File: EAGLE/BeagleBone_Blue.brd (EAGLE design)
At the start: 86.4 x 54.6 mm, 306 parts, among them J2 SERVO_HEADERS_8X, M1 JST_ZH_2, M2 JST_ZH_2, M3 JST_ZH_2, M4 JST_ZH_2, Q1 MOSFET-N, T1 BSS138W-7-F, T2 BSS138W-7-F, U1 TCAN1051HV, U10 TXS0108ERGYR, U13 EMMC, U2 SN74LV1T126DBVR, U3 TPD4S012DRY, U4 TPD4S012DRY, U5 24LC_32AT-I/OT, U6 SN74LVC1G07_DCK_5, U7 WL1835MODGBMOCT, U9 TXS0108ERGYR, X2 SCHA5B0200, X3 USB1, X4 10118192-0001LF, Y1 24 MHz, Y2 32.768kHz

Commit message: EAGLE: more attempts to consolidate library
I tried to rename some parts to eliminate the prefixes added by the exp-lbrs.ulp script.
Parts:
- 0, 1, 2, 3, BT, G, ON, R, WL: device BeagleBone_Blue:LED-0603 -> BeagleBone_Blue:BEAGLEBONE_BLUE_LED-0603
- 5VREG: device BeagleBone_Blue:SO08-TIGHT -> BeagleBone_Blue:BEAGLEBONE_BLUE_SO08-TIGHT
- SIP: device BeagleBone_Blue:OSD3358 -> BeagleBone_Blue:BEAGLEBONE_BLUE_OSD3358
- TP11, TP2, TP3, TP4, TP6, TP7, TP8, TP9: device BeagleBone_Blue:B0,65 -> BeagleBone_Blue:BEAGLEBONE_BLUE_B0,65
- U1: device BeagleBone_Blue:D8 -> BeagleBone_Blue:BEAGLEBONE_BLUE_D8
- U2: device BeagleBone_Blue:SOT23-5 -> BeagleBone_Blue:BEAGLEBONE_BLUE_SOT23-5
- U6: device BeagleBone_Blue:DCK5 -> BeagleBone_Blue:BEAGLEBONE_BLUE_DCK5

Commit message: BRD: update D1, D2, D3 footprints
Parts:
- D1: device adafruit:SOD-123 -> BeagleBone_Blue:ADAFRUIT_SOD-123FL
- D2, D3: device adafruit:SOD-123 -> adafruit:SOD-123FL
- moved D1 12.8 mm to (53.2, 3.17)
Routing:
- net GND: track 226.8 -> 226.2 mm
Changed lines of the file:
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@@
 <grid distance="5" unitdist="mil" unit="mm" style="lines" multiple="1" display="yes" altdistance="0.25" altunitdist="mil" altunit="mm"/>
 <layers>
-<layer number="1" name="Top" color="4" fill="1" visible="no" active="yes"/>
+<layer number="1" name="Top" color="4" fill="1" visible="yes" active="yes"/>
 <layer number="2" name="Route2" color="1" fill="3" visible="no" active="yes"/>
 <layer number="3" name="Route3" color="4" fill="3" visible="no" active="no"/>
@@
 <layer number="14" name="Route14" color="1" fill="6" visible="no" active="no"/>
 <layer number="15" name="Route15" color="4" fill="6" visible="no" active="yes"/>
-<layer number="16" name="Bottom" color="1" fill="1" visible="yes" active="yes"/>
+<layer number="16" name="Bottom" color="1" fill="1" visible="no" active="yes"/>
 <layer number="17" name="Pads" color="2" fill="1" visible="yes" active="yes"/>
 <layer number="18" name="Vias" color="2" fill="1" visible="yes" active="yes"/>
 <layer number="19" name="Unrouted" color="6" fill="1" visible="yes" active="yes"/>
 <layer number="20" name="Dimension" color="15" fill="1" visible="yes" active="yes"/>
-<layer number="21" name="tPlace" color="7" fill="1" visible="no" active="yes"/>
-<layer number="22" name="bPlace" color="7" fill="1" visible="yes" active="yes"/>
-<layer number="23" name="tOrigins" color="15" fill="1" visible="no" active="yes"/>
-<layer number="24" name="bOrigins" color="15" fill="1" visible="yes" active="yes"/>
+<layer number="21" name="tPlace" color="7" fill="1" visible="yes" active="yes"/>
+<layer number="22" name="bPlace" color="7" fill="1" visible="no" active="yes"/>
+<layer number="23" name="tOrigins" color="15" fill="1" visible="yes" active="yes"/>
+<layer number="24" name="bOrigins" color="15" fill="1" visible="no" active="yes"/>
 <layer number="25" name="tNames" color="7" fill="1" visible="no" active="yes"/>
 <layer number="26" name="bNames" color="7" fill="1" visible="no" active="yes"/>
@@
 <layer number="37" name="tTest" color="7" fill="1" visible="no" active="yes"/>
 <layer number="38" name="bTest" color="7" fill="1" visible="no" active="yes"/>
-<layer number="39" name="tKeepout" color="4" fill="11" visible="no" active="yes"/>
-<layer number="40" name="bKeepout" color="1" fill="11" visible="yes" active="yes"/>
-<layer number="41" name="tRestrict" color="4" fill="10" visible="no" active="yes"/>
-<layer number="42" name="bRestrict" color="1" fill="10" visible="yes" active="yes"/>
+<layer number="39" name="tKeepout" color="4" fill="11" visible="yes" active="yes"/>
+<layer number="40" name="bKeepout" color="1" fill="11" visible="no" active="yes"/>
+<layer number="41" name="tRestrict" color="4" fill="10" visible="yes" active="yes"/>
+<layer number="42" name="bRestrict" color="1" fill="10" visible="no" active="yes"/>
 <layer number="43" name="vRestrict" color="2" fill="10" visible="no" active="yes"/>
 <layer number="44" name="Drills" color="7" fill="1" visible="no" active="yes"/>
@@
 <layer number="50" name="dxf" color="7" fill="1" visible="no" active="no"/>
 <layer number="51" name="tDocu" color="7" fill="1" visible="no" active="yes"/>
-<layer number="52" name="bDocu" color="7" fill="1" visible="yes" active="yes"/>
+<layer number="52" name="bDocu" color="7" fill="1" visible="no" active="yes"/>
 <layer number="53" name="tGND_GNDA" color="7" fill="9" visible="no" active="no"/>
 <layer number="54" name="bGND_GNDA" color="1" fill="9" visible="no" active="no"/>
@@
 <attribute name="NAME" x="24.9428" y="-7.493" size="0.8128" layer="25" ratio="6" rot="SR90"/>
 </element>
-<element name="D1" library="adafruit" package="SOD-123" value="" x="51.562" y="-9.525" smashed="yes" rot="MR270">
-<attribute name="NAME" x="53.4494" y="-12.2842" size="0.8128" layer="26" rot="MR0"/>
-<attribute name="VALUE" x="52.846" y="-8.425" size="0.4064" layer="28" rot="MR270"/>
-</element>
 <element name="0" library="BeagleBone_Blue" package="BEAGLEBONE_BLUE_LED-0603" value="BLUE" x="38.735" y="-49.53" smashed="yes" rot="R90">
 <attribute name="NAME" x="41.2496" y="-49.8983" size="1.016" layer="25" rot="R90"/>
@@
 <attribute name="VALUE" x="39.751" y="-43.8785" size="0.8128" layer="27" rot="R180"/>
 </element>
-<element name="D2" library="adafruit" package="SOD-123" value="" x="44.323" y="-5.334" smashed="yes" rot="R90">
+<element name="D2" library="adafruit" package="SOD-123FL" value="" x="44.323" y="-5.334" smashed="yes" rot="R90">
 <attribute name="NAME" x="44.5467" y="-1.9017" size="0.8128" layer="25" rot="R180"/>
 <attribute name="VALUE" x="45.607" y="-6.434" size="0.4064" layer="27" rot="R90"/>
 </element>
-<element name="D3" library="adafruit" package="SOD-123" value="" x="46.0756" y="-5.334" smashed="yes" rot="R90">
+<element name="D3" library="adafruit" package="SOD-123FL" value="" x="46.0756" y="-5.334" smashed="yes" rot="R90">
 <attribute name="NAME" x="46.1088" y="-1.889" size="0.8128" layer="25" rot="R180"/>
 <attribute name="VALUE" x="47.3596" y="-6.434" size="0.4064" layer="27" rot="R90"/>
@@
 <attribute name="VALUE" x="3.4704" y="2.2502" size="1.27" layer="27" rot="R180"/>
 </element>
+<element name="D1" library="BeagleBone_Blue" package="ADAFRUIT_SOD-123FL" value="" x="53.213" y="3.175" rot="MR270"/>
 </elements>
 <signals>
@@
 </signal>
 <signal name="N$16">
-<contactref element="D1" pad="C"/>
 <contactref element="L1" pad="1"/>
 <contactref element="5VREG" pad="2"/>
@@
 <vertex x="43.688" y="-8.382"/>
 </polygon>
+<contactref element="D1" pad="C"/>
 </signal>
 <signal name="I2C2_SCL">
@@
 <contactref element="C3" pad="1"/>
 <contactref element="5VREG" pad="1"/>
-<wire x1="44.323" y1="-7.184" x2="46.0756" y2="-7.184" width="0.8128" layer="1"/>
+<wire x1="44.323" y1="-6.9715" x2="46.0756" y2="-6.9715" width="0.8128" layer="1"/>
 <wire x1="47.752" y1="-8.007" x2="47.25" y2="-8.007" width="0.4064" layer="1"/>
 <wire x1="47.25" y1="-8.007" x2="46.427" y2="-7.184" width="0.4064" layer="1"/>
-<wire x1="46.427" y1="-7.184" x2="46.0756" y2="-7.184" width="0.4064" layer="1"/>
+<wire x1="46.427" y1="-7.184" x2="46.0756" y2="-6.9715" width="0.4064" layer="1"/>
 <wire x1="47.36" y1="-10.5664" x2="47.36" y2="-10.2218" width="0.4064" layer="1"/>
 <wire x1="47.36" y1="-10.2218" x2="47.371" y2="-10.2108" width="0.4064" layer="1"/>
@@
 <contactref element="5VREG" pad="6"/>
 <contactref element="C26" pad="2"/>
-<contactref element="D1" pad="A"/>
 <contactref element="5VREG" pad="7"/>
 <contactref element="5VREG" pad="8"/>
@@
 <wire x1="25.9842" y1="-46.101" x2="25.9842" y2="-45.4406" width="0.1524" layer="16"/>
 <via x="25.9842" y="-45.4406" extent="1-16" drill="0.254" diameter="0.4572"/>
-<wire x1="51.562" y1="-11.375" x2="50.9058" y2="-11.375" width="0.4064" layer="16"/>
 <wire x1="50.9058" y1="-11.375" x2="50.546" y2="-11.7348" width="0.4064" layer="16"/>
 <wire x1="48.2346" y1="-45.0596" x2="48.895" y2="-45.0596" width="0.1524" layer="16"/>
@@
 <wire x1="12.319" y1="-9.271" x2="12.319" y2="-8.509" width="0.254" layer="16"/>
 <via x="12.319" y="-8.509" extent="1-16" drill="0.254"/>
+<contactref element="D1" pad="A"/>
+<wire x1="50.9058" y1="-11.375" x2="53.213" y2="1.5375" width="0" layer="19" extent="16-16"/>
 </signal>
 <signal name="MOT_STBY">
@@
 <wire x1="42.164" y1="-6.985" x2="42.799" y2="-6.35" width="0.1524" layer="1"/>
 <wire x1="45.339" y1="-5.461" x2="46.0756" y2="-4.7244" width="0.6096" layer="1"/>
-<wire x1="46.0756" y1="-4.7244" x2="46.0756" y2="-3.484" width="0.6096" layer="1"/>
+<wire x1="46.0756" y1="-4.7244" x2="46.0756" y2="-3.6965" width="0.6096" layer="1"/>
 <wire x1="42.2148" y1="-6.9342" x2="39.4208" y2="-6.9342" width="0.6096" layer="2"/>
 <wire x1="39.4208" y1="-6.9342" x2="38.862" y2="-7.493" width="0.6096" layer="2"/>

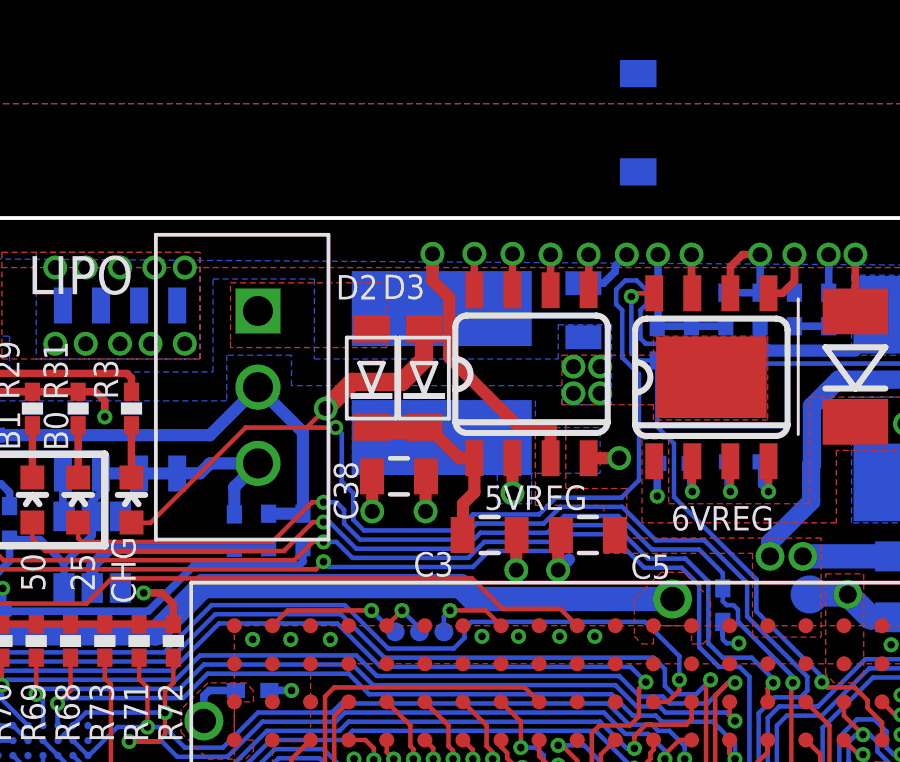
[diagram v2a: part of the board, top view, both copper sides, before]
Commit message: Updated routing for D1, D2 and D3.
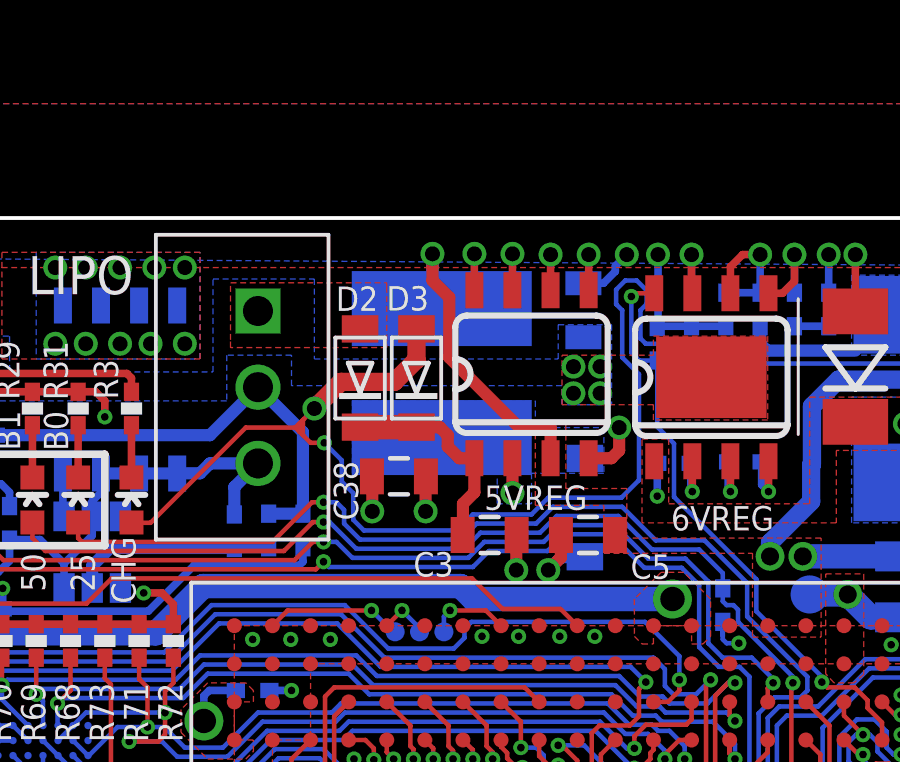
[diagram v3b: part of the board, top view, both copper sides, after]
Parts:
- moved D1 12.9 mm to (51.4, -9.65)
- moved D2 0.38 mm to (43.9, -5.33)
- moved D3 0.25 mm to (45.8, -5.33)
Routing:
- net GND: track 226.2 -> 228.0 mm
- net N$79: track 6.55 -> 7.18 mm

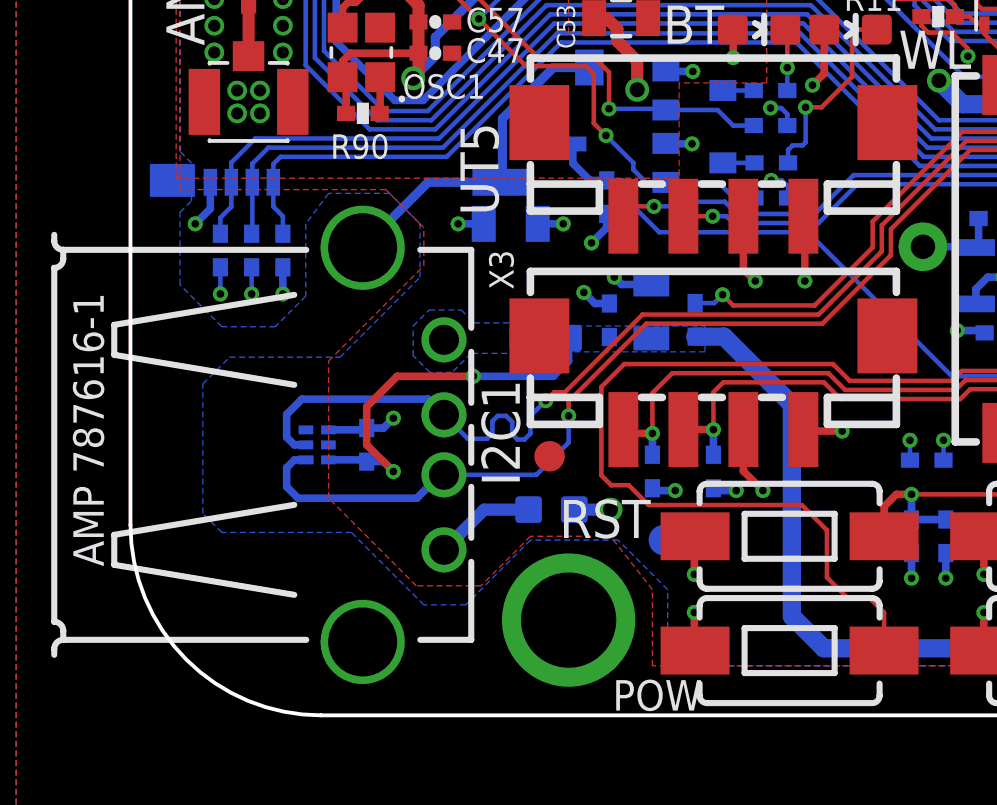
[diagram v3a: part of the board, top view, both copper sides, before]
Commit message: Updated layout around USB connector to allow for more space for wave solder.
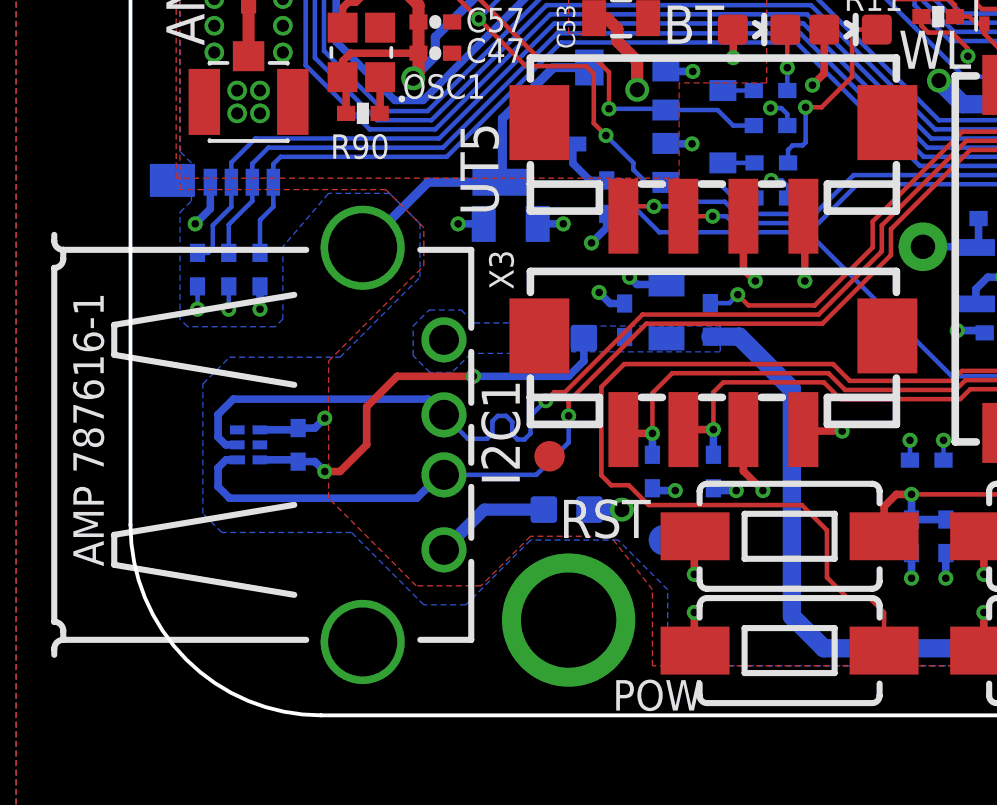
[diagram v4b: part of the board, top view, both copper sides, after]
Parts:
- moved U4 2.29 mm to (3.94, -45.6)
- moved C55 2.29 mm to (5.59, -45.6)
- moved R35 0.99 mm to (4.32, -39.8)
- moved R56 0.99 mm to (2.24, -39.8)
- moved R26 0.99 mm to (3.28, -39.8)
- moved C45 0.51 mm to (16.5, -41.4)
- moved L5 0.51 mm to (14.4, -42.0)
- moved C46 0.51 mm to (17.9, -41.1)
- moved L4 0.51 mm to (14.5, -47.8)
- moved R156 0.51 mm to (19.3, -41.4)
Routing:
- net USB1_D_P: track 64.7 -> 67.0 mm
- net USB1_D_N: track 64.8 -> 67.0 mm
- net N$74: track 48.7 -> 49.9 mm
- net N$5: track 48.1 -> 49.0 mm
- net USB1_VBUS: track 147.1 -> 147.9 mm
- net NTE: track 49.7 -> 50.4 mm
- net N$128: track 3.38 -> 3.88 mm
- net N$129: track 47.5 -> 47.0 mm
